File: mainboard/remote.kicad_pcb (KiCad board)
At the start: 2 copper layers, 185.4 x 109 mm, 46 parts, among them J1 Conn_01x03, J10 Conn_01x03, J11 Conn_01x03, J12 Conn_01x02, J13 Conn_01x04, J14 Conn_01x04, J2 Conn_01x02, J4 Conn_01x03, J5 Conn_01x03, J6 Conn_01x02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

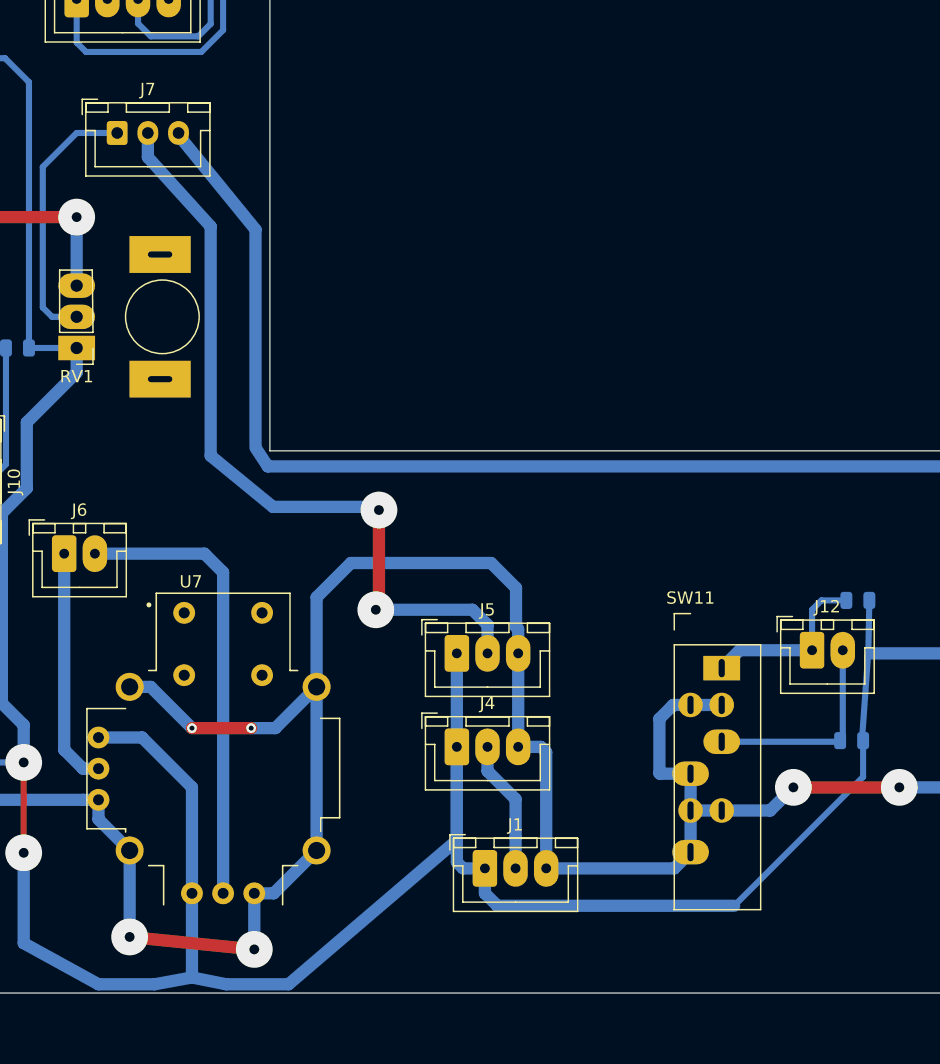
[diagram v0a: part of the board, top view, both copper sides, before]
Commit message: Update for I2C display.
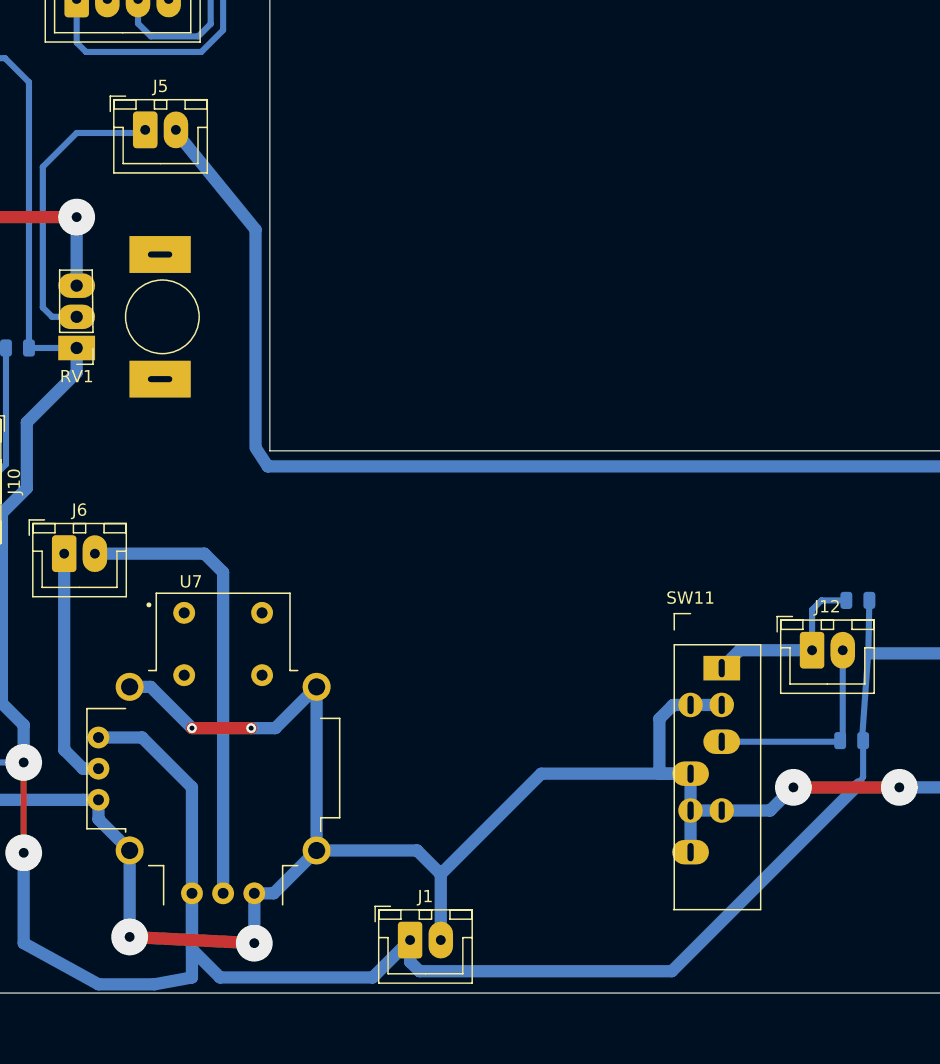
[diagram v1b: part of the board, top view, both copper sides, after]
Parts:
- removed J4, J7: Conn_01x03, Milling:JST_XH_B03B-XH-A_1x03_P2.50mm_Vertical_Milling
- J1, J5: value Conn_01x03 -> Conn_01x02; footprint Milling:JST_XH_B03B-XH-A_1x03_P2.50mm_Vertical_Milling -> Milling:JST_XH_B02B-XH-A_1x02_P2.50mm_Vertical_Milling
- moved J5 49.7 mm to (80.0, 165.4)
- moved J1 8.44 mm to (101.6, 231.4)
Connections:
- J1 pad 2: BAT -> GND
- J5 pad 1: +5V -> A7
- J5 pad 2: A5 -> A6
- RV1 pad 2: A4 -> A7
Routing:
- net A5: track 63.8 -> 0.00 mm, vias 2 -> 0
- net A7: track 0.00 -> 24.1 mm
- net GND: track 653.0 -> 629.7 mm
- net A4: track 21.7 -> 0.00 mm
- net BAT: track 10.9 -> 0.00 mm
- net +5V: track 546.5 -> 541.2 mm

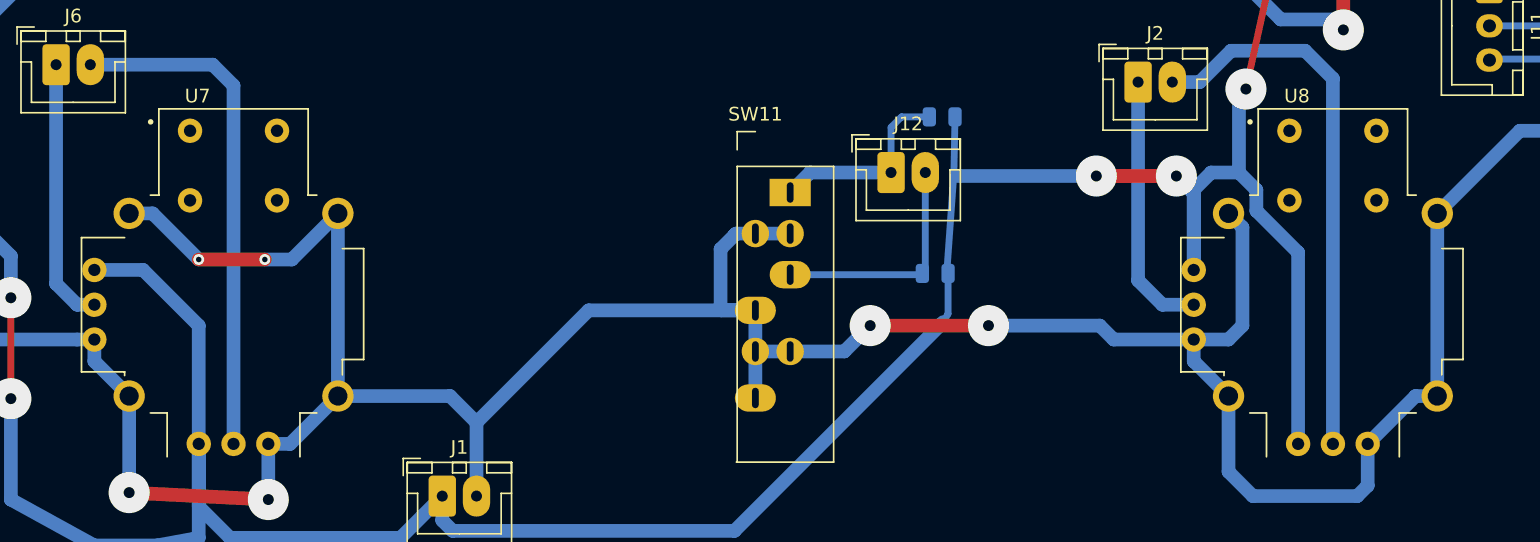
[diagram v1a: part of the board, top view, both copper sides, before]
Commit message: Fix joystick footprint.
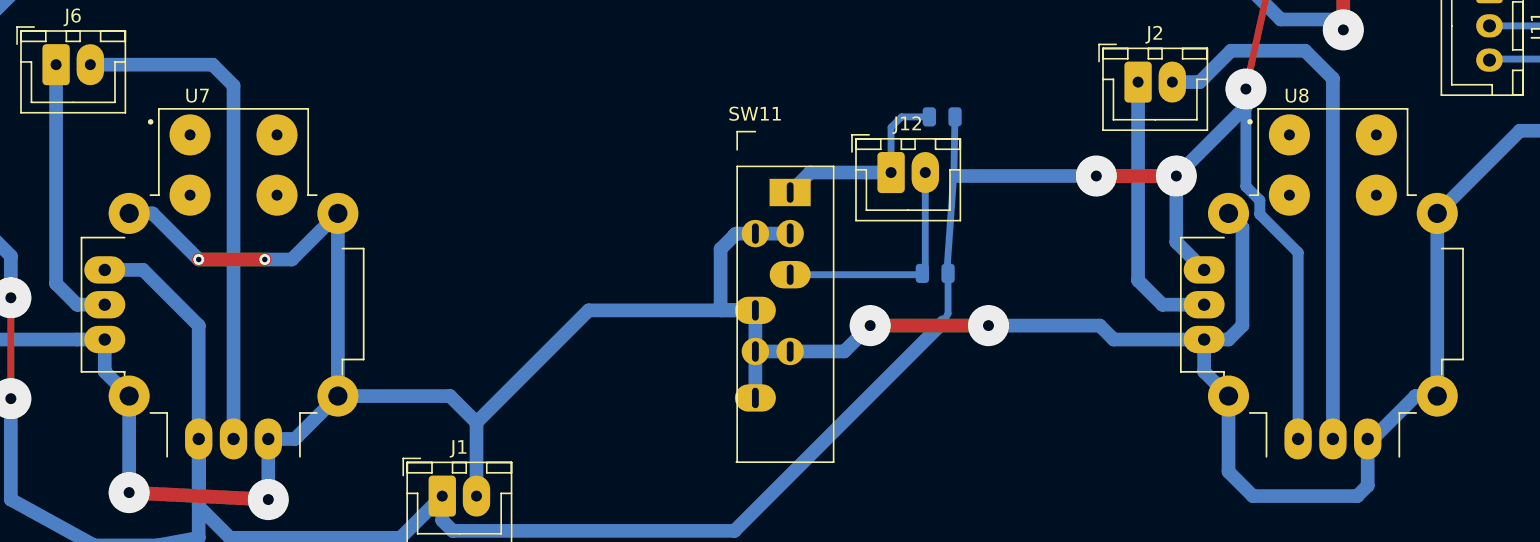
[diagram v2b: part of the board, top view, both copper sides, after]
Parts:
- U7, U8: footprint Remote:XDCR_COM-09032 -> Remote:AnalogJoystick_ALPS_10k
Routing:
- net +5V: track 541.2 -> 540.3 mm
- net GND: track 629.7 -> 628.9 mm

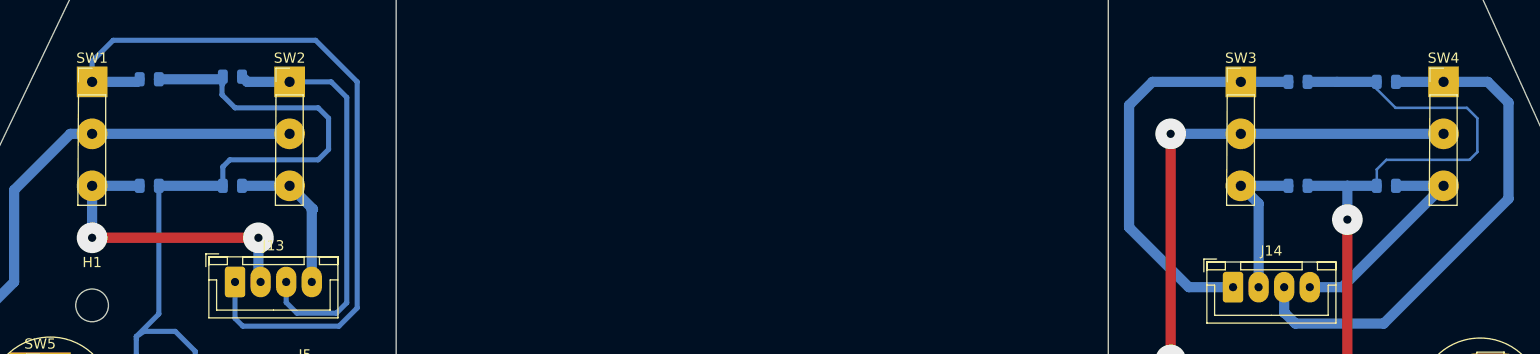
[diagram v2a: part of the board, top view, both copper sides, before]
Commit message: Fix toggle footprints.
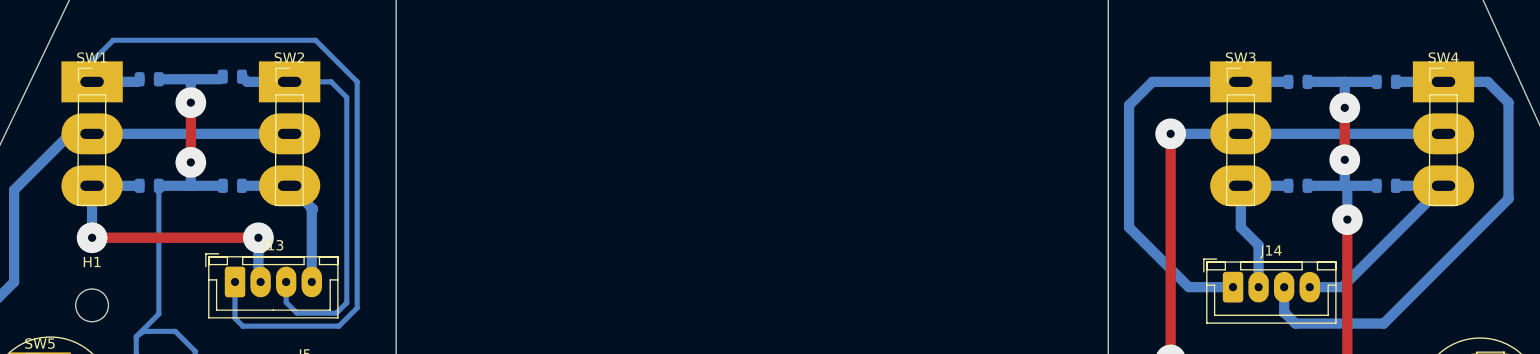
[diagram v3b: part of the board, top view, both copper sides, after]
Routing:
- net +5V: track 540.3 -> 504.7 mm, vias 10 -> 14
